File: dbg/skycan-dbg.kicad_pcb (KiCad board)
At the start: 2 copper layers, 50 x 50 mm, 12 parts, among them J1 DF9_25P_1V_PLUG, J2 DF9_25P_1V_SOCKET, J3 DF9_25P_1V_PLUG, J4 DF9_25P_1V_SOCKET, J5 CONN_13X2, J6 CONN_13X2

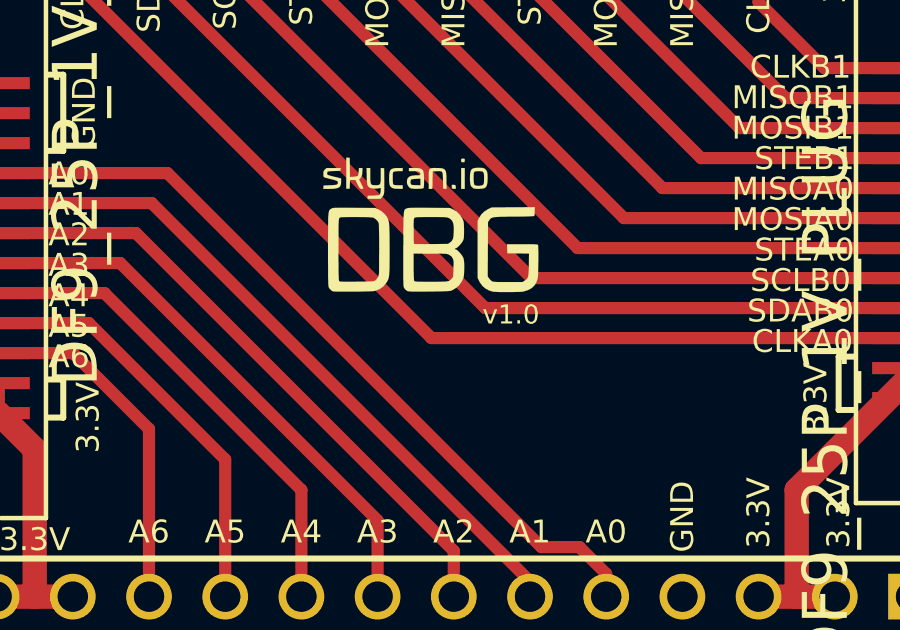
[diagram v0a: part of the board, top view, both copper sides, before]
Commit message: add inner gnd layers for 4 layer dbg board
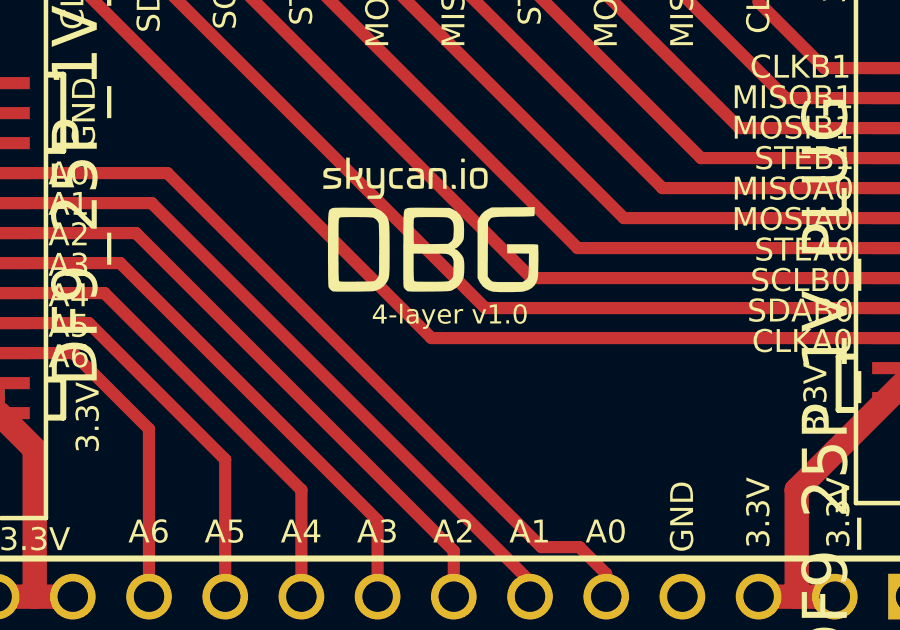
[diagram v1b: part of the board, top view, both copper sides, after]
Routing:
- added copper zone on Inner1.Cu, net GND
- added copper zone on Inner2.Cu, net GND
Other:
- copper layers 2 -> 4
- board text added: "4-layer v1.0"
- board text removed: "v1.0"
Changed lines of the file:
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@@
     (links 125)
     (no_connects 4)
-    (area 99.987299 89.987299 150.012701 140.012701)
+    (area 99.987299 88.8226 150.012701 144.0025)
     (thickness 1.6)
     (drawings 125)
@@
   (layers
     (15 F.Cu signal)
+    (2 Inner2.Cu signal hide)
+    (1 Inner1.Cu signal hide)
     (0 B.Cu signal hide)
     (16 B.Adhes user)
     (17 F.Adhes user)
     (18 B.Paste user)
-    (19 F.Paste user hide)
+    (19 F.Paste user)
     (20 B.SilkS user)
     (21 F.SilkS user)
@@
   (gr_line (start 103.9495 111.252) (end 103.9495 108.712) (angle 90) (layer F.SilkS) (width 0.2))
   (gr_line (start 104.4575 111.252) (end 103.9495 111.252) (angle 90) (layer F.SilkS) (width 0.2))
-  (gr_text v1.0 (at 127 117.221) (layer F.SilkS)
+  (gr_text "4-layer v1.0" (at 124.968 117.221) (layer F.SilkS)
     (effects (font (size 0.635 0.635) (thickness 0.127)))
   )
@@
     (connect_pads (clearance 0.189))
     (min_thickness 0.127)
+    (fill (arc_segments 16) (thermal_gap 0.127) (thermal_bridge_width 0.254))
+    (polygon
+      (pts
+        (xy 150 130) (xy 140 140) (xy 110 140) (xy 100 130) (xy 100 100)
+        (xy 110 90) (xy 140 90) (xy 150 100)
+      )
+    )
+  )
+  (zone (net 11) (net_name GND) (layer Inner2.Cu) (hatch edge 0.508)
+    (connect_pads (clearance 0.189))
+    (min_thickness 0.127)
+    (fill (arc_segments 16) (thermal_gap 0.127) (thermal_bridge_width 0.254))
+    (polygon
+      (pts
+        (xy 150 130) (xy 140 140) (xy 110 140) (xy 100 130) (xy 100 100)
+        (xy 110 90) (xy 140 90) (xy 150 100)
+      )
+    )
+  )
+  (zone (net 11) (net_name GND) (layer Inner1.Cu) (hatch edge 0.508)
+    (connect_pads (clearance 0.189))
+    (min_thickness 0.127)
